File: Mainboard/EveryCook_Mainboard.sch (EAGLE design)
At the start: 100 parts, among them IC1 LM386MM-1, IC2 ATMEGA644A, Q1 8 MHz, Q2 BSP372, Q3 BSP372, T2 ZDT6790, U1 AD7794BRUZ, U4 78M05, U7 CJ1117-3.3

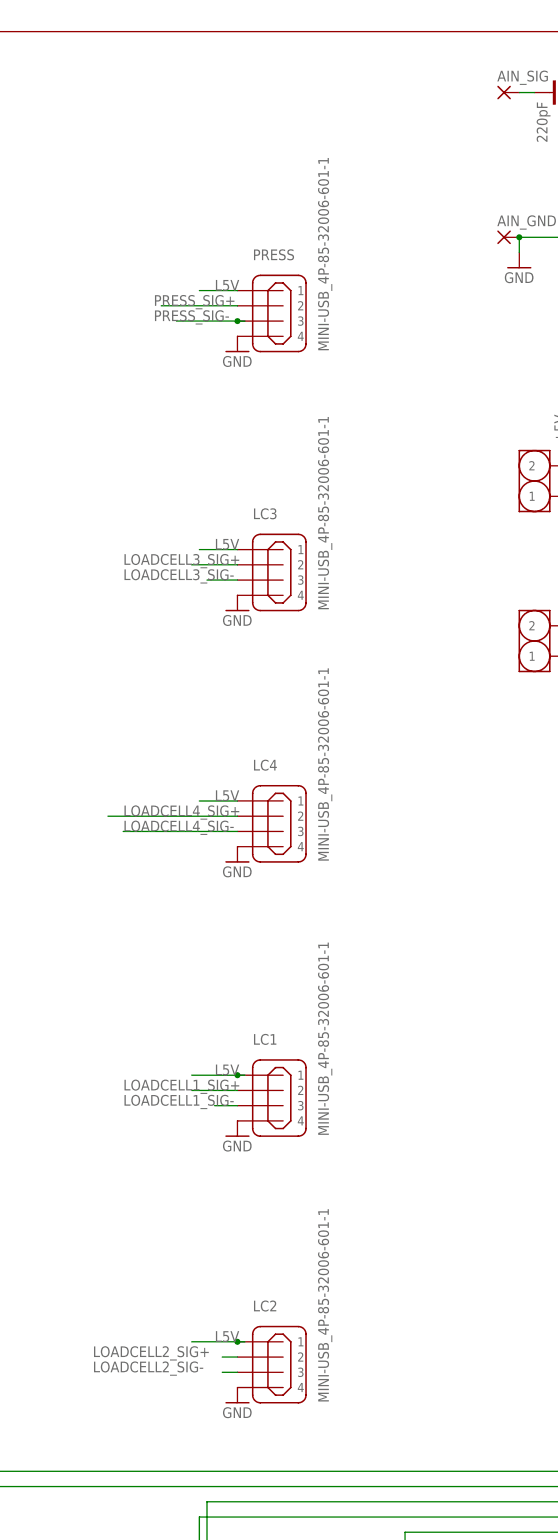
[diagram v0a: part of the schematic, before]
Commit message: Changed USB connectors, created gerber Files
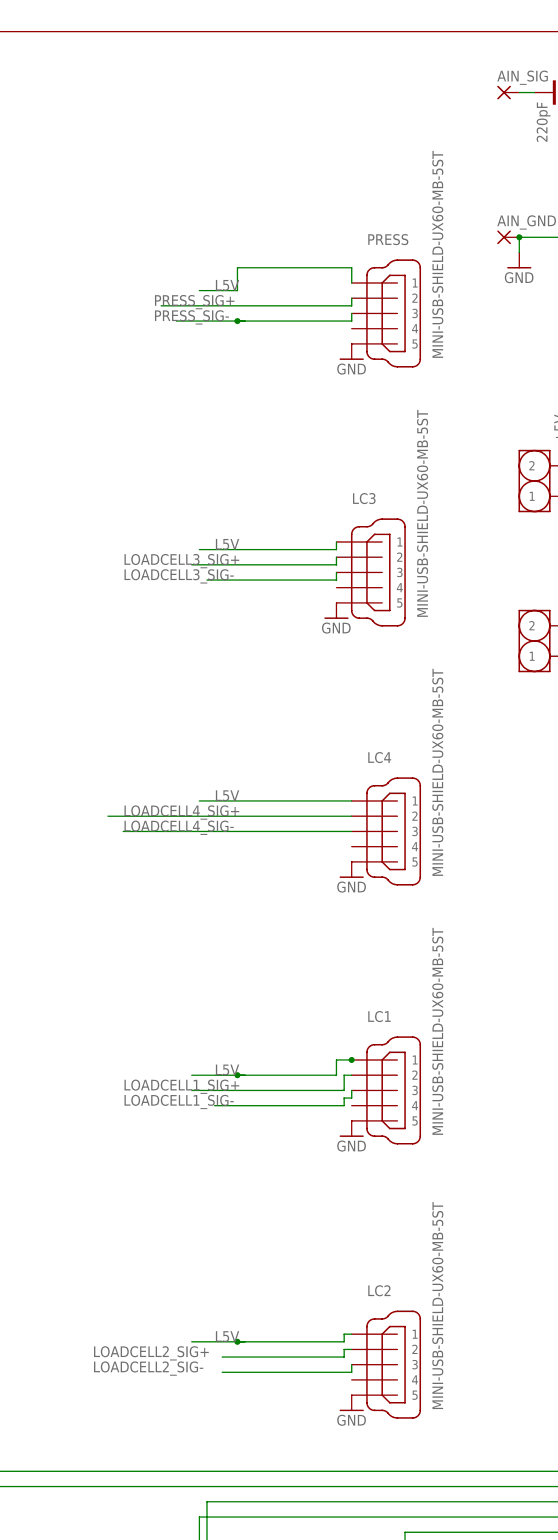
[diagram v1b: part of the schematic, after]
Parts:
- LC1, LC2, LC3, LC4, PRESS: value MINI-USB_4P-85-32006-601-1 -> MINI-USB-SHIELD-UX60-MB-5ST; device con-cypressindustries:MINI-USB_4P-85-32006-601-1 -> con-hirose:MINI-USB-SHIELD-UX60-MB-5ST
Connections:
- net N$55 renamed AT_MISO
- net N$56 renamed AT_MOSI
- net N$8 renamed SCK
- net GND: now also LC1G$1.5, LC2G$1.5, LC3G$1.5, LC4G$1.5, PRESSG$1.5; no longer LC1.4, LC2.4, LC3.4, LC4.4, PRESS.4
- net L5V: now also LC1G$1.1, LC2G$1.1, LC3G$1.1, LC4G$1.1, PRESSG$1.1; no longer LC1.1, LC2.1, LC3.1, LC4.1, PRESS.1
- net LOADCELL1_SIG+: now also LC1G$1.2; no longer LC1.2
- net LOADCELL1_SIG-: now also LC1G$1.3; no longer LC1.3
- net LOADCELL2_SIG+: now also LC2G$1.2; no longer LC2.2
- net LOADCELL2_SIG-: now also LC2G$1.3; no longer LC2.3
- net LOADCELL3_SIG+: now also LC3G$1.2; no longer LC3.2
- net LOADCELL3_SIG-: now also LC3G$1.3; no longer LC3.3
- net LOADCELL4_SIG+: now also LC4G$1.2; no longer LC4.2
- net LOADCELL4_SIG-: now also LC4G$1.3; no longer LC4.3
- net PRESS_SIG+: now also PRESSG$1.2; no longer PRESS.2
- net PRESS_SIG-: now also PRESSG$1.3; no longer PRESS.3

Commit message: Redesign of all boards.
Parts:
- removed AIN_GND, AIN_SIG: (no value), wirepad:2,15/1,0
- removed BUT2, BUT3, C_CLOSE, P_LOCK: (no value), pinhead:PINHD-1X2
- removed RASPI_CONNECTOR_(TOP): (no value), pinhead:PINHD-2X13
- added AIN: (no value), pinhead:PINHD-1X2
- added BUT2+3, CO_CL+PU_LK: (no value), pinhead:PINHD-1X3
- added R9: 270, rcl:R-EU_R0805
- added T3: (no value), transistor:MMBT2222ALT1-NPN-SOT23-BEC
- added U$5: RPI-B-V2, raspberry_mirr:RPI-B-V2
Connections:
- removed net IH_OFF: IC2.(PCINT26/INT0)PD2, POWR_BRD.9
- removed net N$12: I2C.2, RASPI_CONNECTOR_(TOP).3
- removed net N$15: DISPLAY.11, IC2.(PCINT19/TMS)PC3
- removed net N$16: DISPLAY.10, IC2.(PCINT20/TDO)PC4
- removed net N$17: DISPLAY.9, IC2.(PCINT21/TDI)PC5
- removed net N$18: DISPLAY.8, IC2.(PCINT22/TOSC1)PC6
- removed net N$19: DISPLAY.7, IC2.(PCINT23/TOSC2)PC7
- removed net N$37: DISPLAY.6, IC2.(PCINT8/XCK0/T0)PB0
- removed net N$38: DISPLAY.5, IC2.(PCINT9/CLKO/T1)PB1
- removed net N$39: DISPLAY.4, IC2.(PCINT10/INT2/AIN0)PB2
- removed net N$41: DISPLAY.3, IC2.(PCINT11/OC0A/AIN1)PB3
- removed net N$43: DISPLAY.1, IC2.(PCINT12/OC0B/!SS!)PB4
- removed net N$50: I2C.1, RASPI_CONNECTOR_(TOP).5
- removed net N$59: C_CLOSE.1, IC2.(PCINT7/ADC7)PA7
- removed net N$61: IC2.(PCINT5/ADC5)PA5, P_LOCK.1
- new net C_CLOSE: CO_CL+PU_LK.1, IC2.(PCINT7/ADC7)PA7
- new net N$6: I2C.2, U$5.GPIO2/I2C1_SDA
- new net N$8: POWR_BRD.12, T3.C
- new net PB0: DISPLAY.1, IC2.(PCINT8/XCK0/T0)PB0
- new net PB1: DISPLAY.2, IC2.(PCINT9/CLKO/T1)PB1
- new net PB2: DISPLAY.3, IC2.(PCINT10/INT2/AIN0)PB2
- new net PB3: DISPLAY.4, IC2.(PCINT11/OC0A/AIN1)PB3
- new net PC0: DISPLAY.5, IC2.(PCINT16/SCL)PC0
- new net PC1: DISPLAY.6, IC2.(PCINT17/SDA)PC1
- new net PC2: DISPLAY.7, IC2.(PCINT18/TCK)PC2
- new net PC3: DISPLAY.8, IC2.(PCINT19/TMS)PC3
- new net PC4: DISPLAY.9, IC2.(PCINT20/TDO)PC4
- new net PC5: DISPLAY.10, IC2.(PCINT21/TDI)PC5
- new net PC6: DISPLAY.11, IC2.(PCINT22/TOSC1)PC6
- new net PC7: DISPLAY.12, IC2.(PCINT23/TOSC2)PC7
- new net P_LOCK: CO_CL+PU_LK.2, IC2.(PCINT5/ADC5)PA5
- net +3V3: now also IC2.AREF
- net +5V: now also POWR_BRD.11
- net AT_MISO: now also U$5.GPIO23; no longer RASPI_CONNECTOR_(TOP).16
- net AT_MOSI: now also U$5.PWM0/GPIO18; no longer RASPI_CONNECTOR_(TOP).12
- net DAEMON_RST_LINE: now also IC2.(PCINT26/INT0)PD2; no longer IC2.(PCINT16/SCL)PC0
- net GND: now also AIN.1, BUT2+3.3, CO_CL+PU_LK.3, IC2.(PCINT12/OC0B/!SS!)PB4, T3.E, U$5.GND; no longer AIN_GND.P, BUT2.2, BUT3.2, C_CLOSE.2, P_LOCK.2, RASPI_CONNECTOR_(TOP).6
- net MISO: now also U$5.GPIO9/SPI0_MISO; no longer RASPI_CONNECTOR_(TOP).21
- net MOSI: now also U$5.GPIO10/SPI0_MOSI; no longer RASPI_CONNECTOR_(TOP).19
- net N$1: now also I2C.1, U$5.GPIO3/I2C1_SCL; no longer DISPLAY.2, IC2.(PCINT17/SDA)PC1
- net N$11: now also R9.1, T3.B; no longer DISPLAY.12, IC2.(PCINT18/TCK)PC2
- net N$27: now also AIN.2; no longer AIN_SIG.P
- net N$52: now also U$5.UART0_TXD/GPIO14; no longer RASPI_CONNECTOR_(TOP).8
- net N$54: now also U$5.UART0_RXD/GPIO15; no longer RASPI_CONNECTOR_(TOP).10
- net N$58: now also U$5.+5V; no longer RASPI_CONNECTOR_(TOP).2
- net N$62: now also BUT2+3.1, U$5.GPIO7/SPI0_CE1; no longer BUT2.1, RASPI_CONNECTOR_(TOP).24
- net N$63: now also BUT2+3.2, U$5.GPIO8/SPI0_CE0; no longer BUT3.1, RASPI_CONNECTOR_(TOP).26
- net N$64: now also U$5.GPIO25; no longer RASPI_CONNECTOR_(TOP).22
- net RPI_ATMEL_RST: now also U$5.UART0_RTS/GPIO17; no longer RASPI_CONNECTOR_(TOP).11
- net SAFETY_CHAIN: now also R9.2; no longer POWR_BRD.11
- net SCK: now also U$5.GPIO24; no longer RASPI_CONNECTOR_(TOP).18
- net SCLK: now also U$5.GPIO11/SPI0_SLCK; no longer RASPI_CONNECTOR_(TOP).23
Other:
- moved on the sheet: BUT1, DISPLAY, I2C, R47, T2B
